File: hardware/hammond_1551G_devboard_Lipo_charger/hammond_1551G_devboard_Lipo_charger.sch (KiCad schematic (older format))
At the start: 6 parts, among them J1 DevBoardDigital, J2 DevBoardAnalog

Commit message: updated to newer devboard connectors
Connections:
- net labels added: +BATT, VBUS
- net labels removed: VCC
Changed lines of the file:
@@
 EESchema Schematic File Version 4
-LIBS:NiBeetle_JLCPCB_4layer-cache
+LIBS:hammond_1551G_devboard_Lipo_charger-cache
 EELAYER 26 0
 EELAYER END
@@
 $EndComp
 $Comp
-L power:VSS #PWR0105
-U 1 1 5B7AC5E5
-P 2000 2450
-F 0 "#PWR0105" H 2000 2300 50  0001 C CNN
-F 1 "VSS" V 2017 2578 50  0000 L CNN
-F 2 "" H 2000 2450 50  0001 C CNN
-F 3 "" H 2000 2450 50  0001 C CNN
-	1    2000 2450
-	0    1    1    0
-$EndComp
-$Comp
-L power:VSS #PWR0106
-U 1 1 5B7AC5F8
-P 1100 2450
-F 0 "#PWR0106" H 1100 2300 50  0001 C CNN
-F 1 "VSS" V 1118 2578 50  0000 L CNN
-F 2 "" H 1100 2450 50  0001 C CNN
-F 3 "" H 1100 2450 50  0001 C CNN
-	1    1100 2450
-	0    -1   -1   0
-$EndComp
-$Comp
 L power:VDDA #PWR0107
 U 1 1 5B7AC66D
@@
 	0    1    1    0
 $EndComp
-$Comp
-L power:VCC #PWR0111
-U 1 1 5B7AC7C1
-P 2000 2350
-F 0 "#PWR0111" H 2000 2200 50  0001 C CNN
-F 1 "VCC" V 2017 2478 50  0000 L CNN
-F 2 "" H 2000 2350 50  0001 C CNN
-F 3 "" H 2000 2350 50  0001 C CNN
-	1    2000 2350
-	0    1    1    0
-$EndComp
-$Comp
-L power:VCC #PWR0112
-U 1 1 5B7AC7DF
-P 1100 2350
-F 0 "#PWR0112" H 1100 2200 50  0001 C CNN
-F 1 "VCC" V 1118 2477 50  0000 L CNN
-F 2 "" H 1100 2350 50  0001 C CNN
-F 3 "" H 1100 2350 50  0001 C CNN
-	1    1100 2350
-	0    -1   -1   0
-$EndComp
 Wire Wire Line
 	1100 2550 1150 2550
@@
 	1    0    0    -1
 $EndComp
+$Comp
+L power:VBUS #PWR?
+U 1 1 5C4A545D
+P 2000 2350
+F 0 "#PWR?" H 2000 2200 50  0001 C CNN
+F 1 "VBUS" V 2015 2478 50  0000 L CNN
+F 2 "" H 2000 2350 50  0001 C CNN
+F 3 "" H 2000 2350 50  0001 C CNN
+	1    2000 2350
+	0    1    1    0
+$EndComp
+$Comp
+L power:VBUS #PWR?
+U 1 1 5C4A54F6
+P 1100 2350
+F 0 "#PWR?" H 1100 2200 50  0001 C CNN
+F 1 "VBUS" V 1115 2477 50  0000 L CNN
+F 2 "" H 1100 2350 50  0001 C CNN
+F 3 "" H 1100 2350 50  0001 C CNN
+	1    1100 2350
+	0    -1   -1   0
+$EndComp
+$Comp
+L power:+BATT #PWR?
+U 1 1 5C4A5536
+P 1100 2450
+F 0 "#PWR?" H 1100 2300 50  0001 C CNN
+F 1 "+BATT" V 1115 2577 50  0000 L CNN
+F 2 "" H 1100 2450 50  0001 C CNN
+F 3 "" H 1100 2450 50  0001 C CNN
+	1    1100 2450
+	0    -1   -1   0
+$EndComp
+$Comp
+L power:+BATT #PWR?
+U 1 1 5C4A5566
+P 2000 2450
+F 0 "#PWR?" H 2000 2300 50  0001 C CNN
+F 1 "+BATT" V 2015 2578 50  0000 L CNN
+F 2 "" H 2000 2450 50  0001 C CNN
+F 3 "" H 2000 2450 50  0001 C CNN
+	1    2000 2450
+	0    1    1    0
+$EndComp
 $EndSCHEMATC

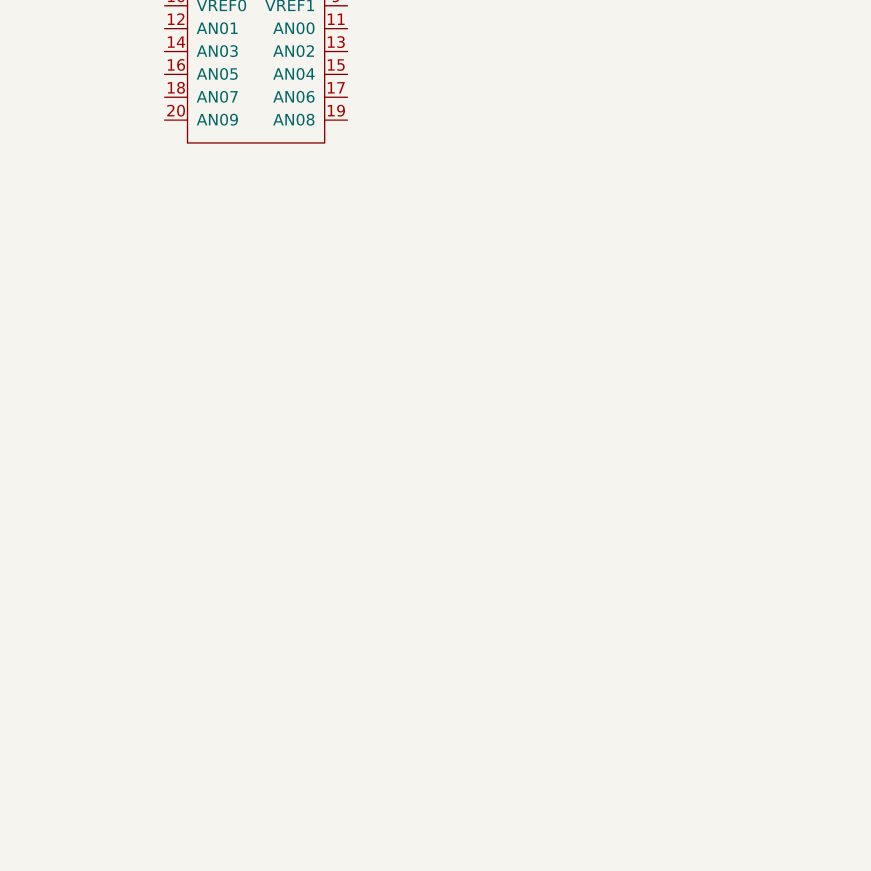
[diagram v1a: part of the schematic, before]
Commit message: new connectors in pcb library, added battery vbus handover schematic
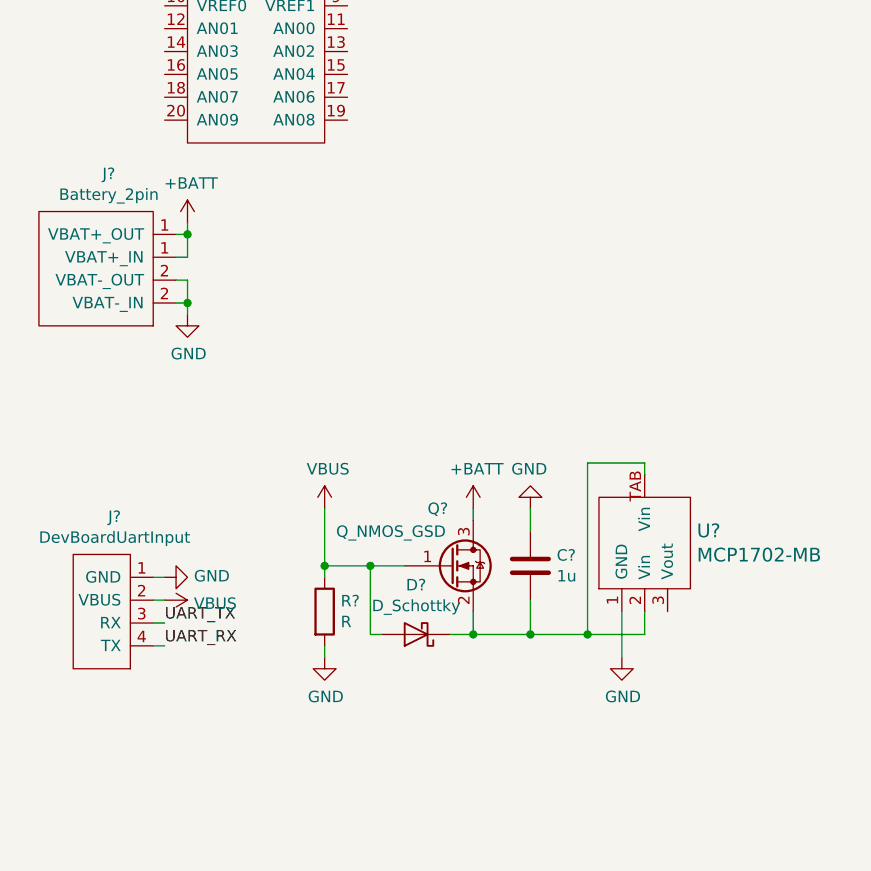
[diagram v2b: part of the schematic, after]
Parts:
- added C?: 1u, SquantorRcl:C_0805, symbol Device:C
- added D?: D_Schottky, symbol Device:D_Schottky
- added J?: Battery_2pin, symbol SquantorConnectors:Battery_2pin
- added J?: DevBoardUartInput, symbol SquantorConnectors:DevBoardUartInput
- added Q?: Q_NMOS_GSD, symbol Device:Q_NMOS_GSD
- added R?: R, SquantorRcl:R_0603_hand, symbol Device:R
- added U?: MCP1702-MB, SquantorIC:SOT89-ViaTab-Microchip-MB, symbol SquantorMicrochip:MCP1702-MB
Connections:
- net +BATT: now also J?.1 (VBAT+_OUT), Q?.3 (D)
- net VBUS: now also D?.2 (A), J?.2 (VBUS), Q?.1 (G), R?.1
- new net: C?.2, D?.1 (K), Q?.2 (S), U?.2 (Vin), U?.TAB (Vin)
- new net GND: C?.1, J?.1 (GND), J?.2 (VBAT-_OUT), R?.2, U?.1 (GND)
- new net UART_RX: J?.4 (TX)
- new net UART_TX: J?.3 (RX)

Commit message: power regulator started and started little bit of layout
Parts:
- added C2: 10u, SquantorRcl:C_0805, symbol Device:C
- added J5: JTAG_2X05, SquantorConnectors:Header-0127-2X05-H006, symbol SquantorConnectors:JTAG_2X05
- D1: renamed from D?; value D_Schottky -> NSR0320; footprint (none) -> SquantorDiodes:SOD-123
- J3: renamed from J?; footprint (none) -> Connector_JST:JST_PH_S2B-PH-K_1x02_P2.00mm_Horizontal
- J4: renamed from J?; footprint (none) -> Connector_JST:JST_PH_S4B-PH-K_1x04_P2.00mm_Horizontal
- Q1: renamed from Q?; footprint (none) -> SquantorIC:SOT23-3-Microchip-TT
- gave numbers to parts that had none: 3
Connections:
- net GND: now also C2.1, J5.1 (VCC), J5.3 (GND), J5.5 (GND), J5.9 (GNDDET)
- net at U1.3 (Vout): now also C2.2
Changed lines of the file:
@@
 $EndComp
 $Comp
-L power:VBUS #PWR?
+L power:VBUS #PWR0105
 U 1 1 5C4A545D
 P 2000 2350
-F 0 "#PWR?" H 2000 2200 50  0001 C CNN
+F 0 "#PWR0105" H 2000 2200 50  0001 C CNN
 F 1 "VBUS" V 2015 2478 50  0000 L CNN
 F 2 "" H 2000 2350 50  0001 C CNN
@@
 $EndComp
 $Comp
-L power:VBUS #PWR?
+L power:VBUS #PWR0106
 U 1 1 5C4A54F6
 P 1100 2350
-F 0 "#PWR?" H 1100 2200 50  0001 C CNN
+F 0 "#PWR0106" H 1100 2200 50  0001 C CNN
 F 1 "VBUS" V 1115 2477 50  0000 L CNN
 F 2 "" H 1100 2350 50  0001 C CNN
@@
 $EndComp
 $Comp
-L power:+BATT #PWR?
+L power:+BATT #PWR0111
 U 1 1 5C4A5536
 P 1100 2450
-F 0 "#PWR?" H 1100 2300 50  0001 C CNN
+F 0 "#PWR0111" H 1100 2300 50  0001 C CNN
 F 1 "+BATT" V 1115 2577 50  0000 L CNN
 F 2 "" H 1100 2450 50  0001 C CNN
@@
 $EndComp
 $Comp
-L power:+BATT #PWR?
+L power:+BATT #PWR0112
 U 1 1 5C4A5566
 P 2000 2450
-F 0 "#PWR?" H 2000 2300 50  0001 C CNN
+F 0 "#PWR0112" H 2000 2300 50  0001 C CNN
 F 1 "+BATT" V 2015 2578 50  0000 L CNN
 F 2 "" H 2000 2450 50  0001 C CNN
@@
 $EndComp
 $Comp
-L SquantorConnectors:Battery_2pin J?
+L SquantorConnectors:Battery_2pin J3
 U 1 1 5C4BC904
 P 850 3900
-F 0 "J?" H 906 4315 50  0000 C CNN
+F 0 "J3" H 906 4315 50  0000 C CNN
 F 1 "Battery_2pin" H 906 4224 50  0000 C CNN
-F 2 "" H 1000 3900 50  0001 C CNN
+F 2 "Connector_JST:JST_PH_S2B-PH-K_1x02_P2.00mm_Horizontal" H 1000 3900 50  0001 C CNN
 F 3 "" H 1000 3900 50  0001 C CNN
 	1    850  3900
@@
 $EndComp
 $Comp
-L SquantorConnectors:DevBoardUartInput J?
+L SquantorConnectors:DevBoardUartInput J4
 U 1 1 5C4BC976
 P 900 5400
-F 0 "J?" H 931 5815 50  0000 C CNN
+F 0 "J4" H 931 5815 50  0000 C CNN
 F 1 "DevBoardUartInput" H 931 5724 50  0000 C CNN
-F 2 "" H 900 5400 50  0001 C CNN
+F 2 "Connector_JST:JST_PH_S4B-PH-K_1x04_P2.00mm_Horizontal" H 900 5400 50  0001 C CNN
 F 3 "" H 900 5400 50  0001 C CNN
 	1    900  5400
@@
 $EndComp
 $Comp
-L power:+BATT #PWR?
+L power:+BATT #PWR0113
 U 1 1 5C4BCA03
 P 1250 3700
-F 0 "#PWR?" H 1250 3550 50  0001 C CNN
+F 0 "#PWR0113" H 1250 3550 50  0001 C CNN
 F 1 "+BATT" H 1265 3873 50  0000 C CNN
 F 2 "" H 1250 3700 50  0001 C CNN
@@
 	1250 3750 1250 3700
 $Comp
-L power:GND #PWR?
+L power:GND #PWR0114
 U 1 1 5C4BCD35
 P 1250 4100
-F 0 "#PWR?" H 1250 3850 50  0001 C CNN
+F 0 "#PWR0114" H 1250 3850 50  0001 C CNN
 F 1 "GND" H 1255 3927 50  0000 C CNN
 F 2 "" H 1250 4100 50  0001 C CNN
@@
 	1250 4050 1250 4100
 $Comp
-L power:GND #PWR?
+L power:GND #PWR0115
 U 1 1 5C4BD15E
 P 1150 5250
-F 0 "#PWR?" H 1150 5000 50  0001 C CNN
+F 0 "#PWR0115" H 1150 5000 50  0001 C CNN
 F 1 "GND" V 1155 5122 50  0000 R CNN
 F 2 "" H 1150 5250 50  0001 C CNN
@@
 $EndComp
 $Comp
-L power:VBUS #PWR?
+L power:VBUS #PWR0116
 U 1 1 5C4BD1D2
 P 1150 5350
-F 0 "#PWR?" H 1150 5200 50  0001 C CNN
+F 0 "#PWR0116" H 1150 5200 50  0001 C CNN
 F 1 "VBUS" V 1165 5478 50  0000 L CNN
 F 2 "" H 1150 5350 50  0001 C CNN
@@
 	1150 5550 1100 5550
 $Comp
-L power:VBUS #PWR?
+L power:VBUS #PWR0117
 U 1 1 5C4BEA24
 P 1850 4950
-F 0 "#PWR?" H 1850 4800 50  0001 C CNN
+F 0 "#PWR0117" H 1850 4800 50  0001 C CNN
 F 1 "VBUS" H 1865 5123 50  0000 C CNN
 F 2 "" H 1850 4950 50  0001 C CNN
@@
 $EndComp
 $Comp
-L power:GND #PWR?
+L power:GND #PWR0118
 U 1 1 5C4BEA77
 P 1850 5600
-F 0 "#PWR?" H 1850 5350 50  0001 C CNN
+F 0 "#PWR0118" H 1850 5350 50  0001 C CNN
 F 1 "GND" H 1855 5427 50  0000 C CNN
 F 2 "" H 1850 5600 50  0001 C CNN
@@
 $EndComp
 $Comp
-L Device:R R?
+L Device:R R1
 U 1 1 5C4BEB15
 P 1850 5400
-F 0 "R?" H 1920 5446 50  0000 L CNN
+F 0 "R1" H 1920 5446 50  0000 L CNN
 F 1 "R" H 1920 5355 50  0000 L CNN
 F 2 "SquantorRcl:R_0603_hand" V 1780 5400 50  0001 C CNN
@@
 	1850 5250 1850 5200
 $Comp
-L Device:D_Schottky D?
+L Device:D_Schottky D1
 U 1 1 5C4BFC51
 P 2250 5500
-F 0 "D?" H 2250 5284 50  0000 C CNN
-F 1 "D_Schottky" H 2250 5375 50  0000 C CNN
-F 2 "" H 2250 5500 50  0001 C CNN
+F 0 "D1" H 2250 5284 50  0000 C CNN
+F 1 "NSR0320" H 2250 5375 50  0000 C CNN
+F 2 "SquantorDiodes:SOD-123" H 2250 5500 50  0001 C CNN
 F 3 "~" H 2250 5500 50  0001 C CNN
 	1    2250 5500
@@
 	1850 5200 1850 4950
 $Comp
-L Device:Q_NMOS_GSD Q?
+L Device:Q_NMOS_GSD Q1
 U 1 1 5C4C02A6
 P 2400 5200
-F 0 "Q?" H 2300 5450 50  0000 L CNN
+F 0 "Q1" H 2300 5450 50  0000 L CNN
 F 1 "Q_NMOS_GSD" H 1900 5350 50  0000 L CNN
-F 2 "" H 2600 5300 50  0001 C CNN
+F 2 "SquantorIC:SOT23-3-Microchip-TT" H 2600 5300 50  0001 C CNN
 F 3 "~" H 2400 5200 50  0001 C CNN
 	1    2400 5200
@@
 	2500 5500 2500 5400
 $Comp
-L power:+BATT #PWR?
+L power:+BATT #PWR0119
 U 1 1 5C4C2417
 P 2500 4950
-F 0 "#PWR?" H 2500 4800 50  0001 C CNN
+F 0 "#PWR0119" H 2500 4800 50  0001 C CNN
 F 1 "+BATT" H 2515 5123 50  0000 C CNN
 F 2 "" H 2500 4950 50  0001 C CNN
@@
 	2500 5000 2500 4950
 $Comp
-L SquantorMicrochip:MCP1702-MB U?
+L SquantorMicrochip:MCP1702-MB U1
 U 1 1 5C4C33E8
 P 3250 5100
-F 0 "U?" V 3303 4872 60  0000 R CNN
-F 1 "MCP1702-MB" V 3197 4872 60  0000 R CNN
+F 0 "U1" V 3550 5050 60  0000 R CNN
+F 1 "MCP1702-MB" V 3700 5400 60  0000 R CNN
 F 2 "SquantorIC:SOT89-ViaTab-Microchip-MB" H 3250 5100 60  0001 C CNN
 F 3 "" H 3250 5100 60  0001 C CNN
@@
 $EndComp
 $Comp
-L power:GND #PWR?
+L power:GND #PWR0120
 U 1 1 5C4C349D
 P 3150 5600
-F 0 "#PWR?" H 3150 5350 50  0001 C CNN
+F 0 "#PWR0120" H 3150 5350 50  0001 C CNN
 F 1 "GND" H 3155 5427 50  0000 C CNN
 F 2 "" H 3150 5600 50  0001 C CNN
@@
 	3000 5500 3250 5500
 $Comp
-L Device:C C?
+L Device:C C1
 U 1 1 5C4C67F4
 P 2750 5200
-F 0 "C?" H 2865 5246 50  0000 L CNN
+F 0 "C1" H 2865 5246 50  0000 L CNN
 F 1 "1u" H 2865 5155 50  0000 L CNN
 F 2 "SquantorRcl:C_0805" H 2788 5050 50  0001 C CNN
@@
 $EndComp
 $Comp
-L power:GND #PWR?
+L power:GND #PWR0121
 U 1 1 5C4C6846
 P 2750 4950
-F 0 "#PWR?" H 2750 4700 50  0001 C CNN
+F 0 "#PWR0121" H 2750 4700 50  0001 C CNN
 F 1 "GND" H 2755 4777 50  0000 C CNN
 F 2 "" H 2750 4950 50  0001 C CNN
@@
 Wire Wire Line
 	2750 5050 2750 4950
+Wire Wire Line
+	3350 5400 3350 5500
+Wire Wire Line
+	3350 5500 3600 5500
+$Comp
+L Device:C C2
+U 1 1 5C4CA5C4
+P 3600 5200
+F 0 "C2" H 3715 5246 50  0000 L CNN
+F 1 "10u" H 3715 5155 50  0000 L CNN
+F 2 "SquantorRcl:C_0805" H 3638 5050 50  0001 C CNN
+F 3 "~" H 3600 5200 50  0001 C CNN
+	1    3600 5200
+	1    0    0    -1
+$EndComp
+$Comp
+L power:GND #PWR0122
+U 1 1 5C4CA7DE
+P 3600 4950
+F 0 "#PWR0122" H 3600 4700 50  0001 C CNN
+F 1 "GND" H 3605 4777 50  0000 C CNN
+F 2 "" H 3600 4950 50  0001 C CNN
+F 3 "" H 3600 4950 50  0001 C CNN
+	1    3600 4950
+	-1   0    0    1
+$EndComp
+Wire Wire Line
+	3600 5350 3600 5500
+Wire Wire Line
+	3600 5050 3600 4950
+$Comp
+L SquantorConnectors:JTAG_2X05 J5
+U 1 1 5C4CBB75
+P 1600 6450
+F 0 "J5" H 1600 6937 60  0000 C CNN
+F 1 "JTAG_2X05" H 1600 6831 60  0000 C CNN
+F 2 "SquantorConnectors:Header-0127-2X05-H006" H 1600 6600 60  0001 C CNN
+F 3 "" H 1600 6600 60  0001 C CNN
+	1    1600 6450
+	1    0    0    -1
+$EndComp
+$Comp
+L power:GND #PWR0123
+U 1 1 5C4CBC11
+P 2150 6700
+F 0 "#PWR0123" H 2150 6450 50  0001 C CNN
+F 1 "GND" H 2155 6527 50  0000 C CNN
+F 2 "" H 2150 6700 50  0001 C CNN
+F 3 "" H 2150 6700 50  0001 C CNN
+	1    2150 6700
+	1    0    0    -1
+$EndComp
+Wire Wire Line
+	2100 6250 2150 6250
+Wire Wire Line
+	2100 6650 2150 6650
+Connection ~ 2150 6650
+Wire Wire Line
+	2150 6650 2150 6700
+Wire Wire Line
+	2150 6250 2150 6350
+Wire Wire Line
+	2100 6450 2150 6450
+Connection ~ 2150 6450
+Wire Wire Line
+	2150 6450 2150 6650
+Wire Wire Line
+	2100 6350 2150 6350
+Connection ~ 2150 6350
+Wire Wire Line
+	2150 6350 2150 6450
 $EndSCHEMATC

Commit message: further schematic layout with power joining and some experiments
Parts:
- added U2, U3, U4, U5: power_joiner_2_nets, SquantorSpecial:power_joiner_2_conn_06mm, symbol SquantorSpecial:power_joiner_2_nets
- J3: symbol SquantorConnectors:Battery_2pin -> SquantorConnectors:batt_recharge
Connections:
- net UART_TX is gone; now on an unnamed net: J4.3 (RX)
- net GND: now also U2.1, U3.1
- net VDD: now also U5.2
- net VDDA: now also U4.2
- net VSS: now also U2.2
- net VSSA: now also U3.2
- net at C2.2, U1.3 (Vout): now also U4.1, U5.1
- net UART_RX: no longer names the net of J4.4 (TX)
- no-connect marks 0 -> 33
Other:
- moved on the sheet: C1, C2, D1, J1, J2, J4, J5, Q1, R1, U1

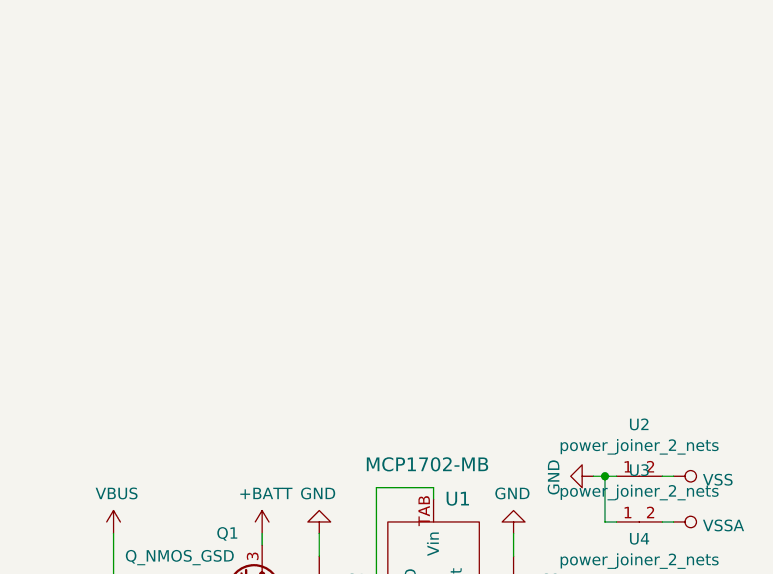
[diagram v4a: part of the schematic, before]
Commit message: added lipo charging schematic, starting initial layout on pcb
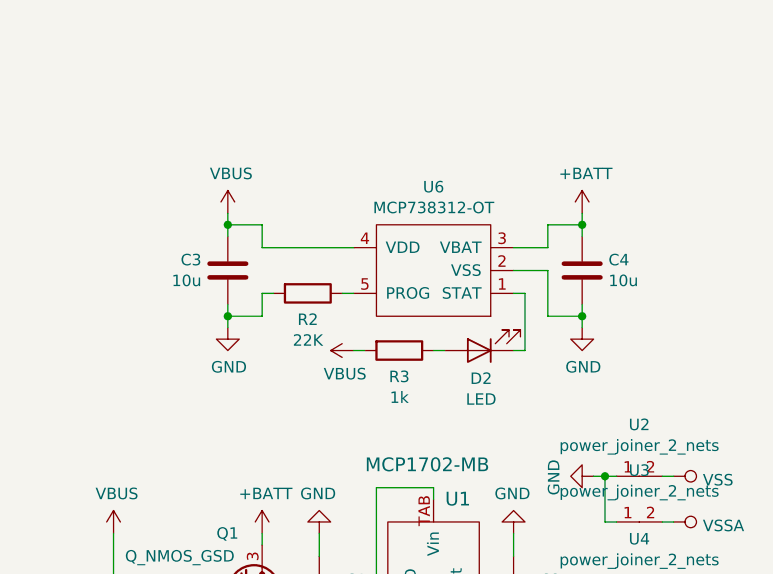
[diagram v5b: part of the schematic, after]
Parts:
- added C3, C4: 10u, SquantorRcl:C_0805, symbol Device:C
- added D2: LED, LED_SMD:LED_0603_1608Metric_Pad1.05x0.95mm_HandSolder, symbol Device:LED
- added R2: 22K, SquantorRcl:R_0603_hand, symbol Device:R
- added R3: 1k, SquantorRcl:R_0603_hand, symbol Device:R
- added U6: MCP738312-OT, SquantorIC:SOT23-5-Microchip-OT, symbol SquantorMicrochip:MCP738312-OT
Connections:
- net +BATT: now also C4.1, U6.3 (VBAT)
- net GND: now also C3.2, C4.2, R2.2, U6.2 (VSS)
- net VBUS: now also C3.1, R3.2, U6.4 (VDD)
- new net: D2.1 (K), U6.1 (STAT)
- new net: R2.1, U6.5 (PROG)
- new net: D2.2 (A), R3.1
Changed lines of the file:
@@
 Wire Wire Line
 	1750 3650 1700 3650
+$Comp
+L SquantorMicrochip:MCP738312-OT U6
+U 1 1 5C51254D
+P 4650 3850
+F 0 "U6" H 4650 3485 50  0000 C CNN
+F 1 "MCP738312-OT" H 4650 3576 50  0000 C CNN
+F 2 "SquantorIC:SOT23-5-Microchip-OT" H 4500 3850 50  0001 C CNN
+F 3 "" H 4500 3850 50  0001 C CNN
+	1    4650 3850
+	-1   0    0    1
+$EndComp
+$Comp
+L power:VBUS #PWR0129
+U 1 1 5C5125D5
+P 3750 3600
+F 0 "#PWR0129" H 3750 3450 50  0001 C CNN
+F 1 "VBUS" H 3765 3773 50  0000 C CNN
+F 2 "" H 3750 3600 50  0001 C CNN
+F 3 "" H 3750 3600 50  0001 C CNN
+	1    3750 3600
+	1    0    0    -1
+$EndComp
+$Comp
+L Device:C C3
+U 1 1 5C51489A
+P 3750 3850
+F 0 "C3" H 3635 3896 50  0000 R CNN
+F 1 "10u" H 3635 3805 50  0000 R CNN
+F 2 "SquantorRcl:C_0805" H 3788 3700 50  0001 C CNN
+F 3 "~" H 3750 3850 50  0001 C CNN
+	1    3750 3850
+	1    0    0    -1
+$EndComp
+$Comp
+L power:GND #PWR0130
+U 1 1 5C516BAB
+P 3750 4100
+F 0 "#PWR0130" H 3750 3850 50  0001 C CNN
+F 1 "GND" H 3755 3927 50  0000 C CNN
+F 2 "" H 3750 4100 50  0001 C CNN
+F 3 "" H 3750 4100 50  0001 C CNN
+	1    3750 4100
+	1    0    0    -1
+$EndComp
+Wire Wire Line
+	3750 3600 3750 3650
+Wire Wire Line
+	3750 4000 3750 4050
+Wire Wire Line
+	4300 3750 3900 3750
+Wire Wire Line
+	3900 3750 3900 3650
+Wire Wire Line
+	3900 3650 3750 3650
+Connection ~ 3750 3650
+Wire Wire Line
+	3750 3650 3750 3700
+$Comp
+L Device:R R2
+U 1 1 5C51A207
+P 4100 3950
+F 0 "R2" V 4215 3950 50  0000 C CNN
+F 1 "22K" V 4306 3950 50  0000 C CNN
+F 2 "SquantorRcl:R_0603_hand" V 4030 3950 50  0001 C CNN
+F 3 "~" H 4100 3950 50  0001 C CNN
+	1    4100 3950
+	0    1    1    0
+$EndComp
+Wire Wire Line
+	3950 3950 3900 3950
+Wire Wire Line
+	3900 3950 3900 4050
+Wire Wire Line
+	3900 4050 3750 4050
+Connection ~ 3750 4050
+Wire Wire Line
+	3750 4050 3750 4100
+Wire Wire Line
+	4250 3950 4300 3950
+$Comp
+L power:GND #PWR0131
+U 1 1 5C52015D
+P 5300 4100
+F 0 "#PWR0131" H 5300 3850 50  0001 C CNN
+F 1 "GND" H 5305 3927 50  0000 C CNN
+F 2 "" H 5300 4100 50  0001 C CNN
+F 3 "" H 5300 4100 50  0001 C CNN
+	1    5300 4100
+	1    0    0    -1
+$EndComp
+$Comp
+L Device:C C4
+U 1 1 5C520194
+P 5300 3850
+F 0 "C4" H 5415 3896 50  0000 L CNN
+F 1 "10u" H 5415 3805 50  0000 L CNN
+F 2 "SquantorRcl:C_0805" H 5338 3700 50  0001 C CNN
+F 3 "~" H 5300 3850 50  0001 C CNN
+	1    5300 3850
+	1    0    0    -1
+$EndComp
+$Comp
+L power:+BATT #PWR0132
+U 1 1 5C520275
+P 5300 3600
+F 0 "#PWR0132" H 5300 3450 50  0001 C CNN
+F 1 "+BATT" H 5315 3773 50  0000 C CNN
+F 2 "" H 5300 3600 50  0001 C CNN
+F 3 "" H 5300 3600 50  0001 C CNN
+	1    5300 3600
+	1    0    0    -1
+$EndComp
+Wire Wire Line
+	5300 4100 5300 4050
+Wire Wire Line
+	5300 3700 5300 3650
+Wire Wire Line
+	5000 3750 5150 3750
+Wire Wire Line
+	5150 3750 5150 3650
+Wire Wire Line
+	5150 3650 5300 3650
+Connection ~ 5300 3650
+Wire Wire Line
+	5300 3650 5300 3600
+Wire Wire Line
+	5300 4050 5150 4050
+Wire Wire Line
+	5150 4050 5150 3850
+Wire Wire Line
+	5150 3850 5000 3850
+Connection ~ 5300 4050
+Wire Wire Line
+	5300 4050 5300 4000
+$Comp
+L Device:R R3
+U 1 1 5C5281E1
+P 4500 4200
+F 0 "R3" V 4615 4200 50  0000 C CNN
+F 1 "1k" V 4706 4200 50  0000 C CNN
+F 2 "SquantorRcl:R_0603_hand" V 4430 4200 50  0001 C CNN
+F 3 "~" H 4500 4200 50  0001 C CNN
+	1    4500 4200
+	0    1    1    0
+$EndComp
+$Comp
+L Device:LED D2
+U 1 1 5C528327
+P 4850 4200
+F 0 "D2" H 4842 4323 50  0000 C CNN
+F 1 "LED" H 4842 4414 50  0000 C CNN
+F 2 "LED_SMD:LED_0603_1608Metric_Pad1.05x0.95mm_HandSolder" H 4850 4200 50  0001 C CNN
+F 3 "~" H 4850 4200 50  0001 C CNN
+	1    4850 4200
+	-1   0    0    1
+$EndComp
+$Comp
+L power:VBUS #PWR0133
+U 1 1 5C52842C
+P 4300 4200
+F 0 "#PWR0133" H 4300 4050 50  0001 C CNN
+F 1 "VBUS" V 4197 4237 50  0000 C CNN
+F 2 "" H 4300 4200 50  0001 C CNN
+F 3 "" H 4300 4200 50  0001 C CNN
+	1    4300 4200
+	0    -1   -1   0
+$EndComp
+Wire Wire Line
+	4300 4200 4350 4200
+Wire Wire Line
+	4650 4200 4700 4200
+Wire Wire Line
+	5000 4200 5050 4200
+Wire Wire Line
+	5050 4200 5050 3950
+Wire Wire Line
+	5050 3950 5000 3950
 $EndSCHEMATC

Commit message: further placement/layout, included newer PCB library
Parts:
- D1: footprint SquantorDiodes:SOD-123 -> SquantorDiodes:SOD_323_onsemi
- Q1: footprint SquantorIC:SOT23-3-Microchip-TT -> SquantorIC:SOT23-3
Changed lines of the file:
@@
 F 0 "D1" H 3650 5334 50  0000 C CNN
 F 1 "NSR0320" H 3650 5425 50  0000 C CNN
-F 2 "SquantorDiodes:SOD-123" H 3650 5550 50  0001 C CNN
+F 2 "SquantorDiodes:SOD_323_onsemi" H 3650 5550 50  0001 C CNN
 F 3 "~" H 3650 5550 50  0001 C CNN
 	1    3650 5550
@@
 F 0 "Q1" H 3700 5500 50  0000 L CNN
 F 1 "Q_NMOS_GSD" H 3300 5400 50  0000 L CNN
-F 2 "SquantorIC:SOT23-3-Microchip-TT" H 4000 5350 50  0001 C CNN
+F 2 "SquantorIC:SOT23-3" H 4000 5350 50  0001 C CNN
 F 3 "~" H 3800 5250 50  0001 C CNN
 	1    3800 5250
